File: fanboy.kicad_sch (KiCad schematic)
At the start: 51 parts, among them J1 XT30, J2 USB_C_Receptacle_USB2.0, J3 Conn_01x04, J4 Conn_01x04, SW1 GT-TC029B-H025-L1N, SW2 GT-TC029B-H025-L1N, U1 TPD1E05U06DYA, U2 TPD1E05U06DYA, U3 W25Q16JVUXIQ TR, U4 TLV1117LV33DCYR, U5 EMC2302, U6 RP2040, U7 SK6812, Y1 12MHz

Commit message: finished routing, added render and readme
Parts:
- removed C1, C2: 30pF, Capacitor_SMD:C_0402_1005Metric, symbol Device:C
- removed C10, C3, C5, C9: 1uF, Capacitor_SMD:C_0402_1005Metric, symbol Device:C
- removed C11, C12, C13, C15, C16, C17, C18, C4, C7, C8: 0.1uF, Capacitor_SMD:C_0402_1005Metric, symbol Device:C
- removed D1: SMAJ6.0A, Diode_SMD:D_SMB, symbol Diode:SMAJ6.0A
- removed J2: USB_C_Receptacle_USB2.0, aditBoard:USB_C_Receptacle_GCT_USB4105-xx-A_16P_TopMnt_Horizontal, symbol aditBoard:USB_C_Receptacle_USB2.0
- removed R1: 10k, Resistor_SMD:R_0402_1005Metric, symbol Device:R_US
- removed R11, R12: 4.7k, Resistor_SMD:R_0402_1005Metric, symbol Device:R_US
- removed R2, R3: 5.1k, Resistor_SMD:R_0402_1005Metric, symbol Device:R_US
- removed R4: 1k, Resistor_SMD:R_0402_1005Metric, symbol Device:R_US
- removed R5: 49.9k, Resistor_SMD:R_0402_1005Metric, symbol Device:R_US
- removed R7, R8: 33, Resistor_SMD:R_0402_1005Metric, symbol Device:R_US
- removed TP4: TestPoint, TestPoint:TestPoint_Pad_D1.0mm, symbol Connector:TestPoint
- removed U1, U2: TPD1E05U06DYA, Diode_SMD:D_SOD-523, symbol Power_Protection:TPD1E05U06DYA
- removed U3: W25Q16JVUXIQ TR, emberone:USON-8_UX_2x3x0p6_WIN, symbol emberone:W25Q16JVUXIQ_TR
- removed U4: TLV1117LV33DCYR, emberone:VREG_TLV1117LV33DCYR, symbol emberone:TLV1117LV33DCYR
- removed U6: RP2040, Package_DFN_QFN:QFN-56-1EP_7x7mm_P0.4mm_EP3.2x3.2mm, symbol aditBoard:RP2040
- removed U7: SK6812, emberone:LED-SMD_4P-L4.0-W1.6-L, symbol athvfd:SK6812SIDE-A-RVS
- added C100, C101, C104, C105, C106, C107, C108, C109, C110, C99: 0.1uF, Capacitor_SMD:C_0402_1005Metric, symbol Device:C
- added C102, C103, C90, C98: 1uF, Capacitor_SMD:C_0402_1005Metric, symbol Device:C
- added C96, C97: 30pF, Capacitor_SMD:C_0402_1005Metric, symbol Device:C
- added J6: USB_C_Receptacle_USB2.0, aditBoard:USB_C_Receptacle_GCT_USB4105-xx-A_16P_TopMnt_Horizontal, symbol aditBoard:USB_C_Receptacle_USB2.0
- added R19, R20: 4.7k, Resistor_SMD:R_0402_1005Metric, symbol Device:R_US
- added R34: 49.9k, Resistor_SMD:R_0402_1005Metric, symbol Device:R_US
- added R50: 10k, Resistor_SMD:R_0402_1005Metric, symbol Device:R_US
- added R51, R52: 5.1k, Resistor_SMD:R_0402_1005Metric, symbol Device:R_US
- added R53, R54: 33, Resistor_SMD:R_0402_1005Metric, symbol Device:R_US
- added R55: 1k, Resistor_SMD:R_0402_1005Metric, symbol Device:R_US
- added TP1, TP2: TestPoint, TestPoint:TestPoint_Pad_D1.0mm, symbol Connector:TestPoint
- added U10: TLV1117LV33DCYR, emberone:VREG_TLV1117LV33DCYR, symbol emberone:TLV1117LV33DCYR
- added U27: RP2040, Package_DFN_QFN:QFN-56-1EP_7x7mm_P0.4mm_EP3.2x3.2mm, symbol aditBoard:RP2040
- added U8: W25Q16JVUXIQ TR, emberone:USON-8_UX_2x3x0p6_WIN, symbol emberone:W25Q16JVUXIQ_TR
- added U9: SK6812, emberone:LED-SMD_4P-L4.0-W1.6-L, symbol athvfd:SK6812SIDE-A-RVS
- renumbered SW2 to SW1, SW1 to SW2
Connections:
- net 1V1: now also C100.2, C101.2, C102.2, U27.23 (DVDD), U27.45 (VREG_VOUT), U27.50 (DVDD)
- net 3V3: now also C103.2, C104.2, C105.2, C106.2, C107.2, C108.2, C109.2, C110.2, C98.1, C99.2, R19.1, R20.2, R34.2, R50.1, U10.2 (VOUT), U10.4 (VOUT), U27.1 (IOVDD), U27.10 (IOVDD), U27.22 (IOVDD), U27.33 (IOVDD), U27.42 (IOVDD), U27.43 (ADC_AVDD), U27.44 (VREG_IN), U27.48 (USB_VDD), U27.49 (IOVDD), U8.8 (VCC)
- net 5V: now also C90.1, J6.A4B9 (VBUS), J6.B4A9 (VBUS), U10.3 (VIN), U9.2 (VDD)
- net GND: now also TP3.1, C100.1, C101.1, C102.1, C103.1, C104.1, C105.1, C106.1, C107.1, C108.1, C109.1, C110.1, C90.2, C96.1, C97.1, C98.2, C99.1, J6.A1B12 (GND), J6.B1A12 (GND), J6.S1 (SHIELD), R51.1, R52.1, U10.1 (GND), U27.19 (TESTEN), U27.57 (GND), U8.4 (GND), U8.9 (EPAD), U9.4 (GND)
- net QSPI_SCLK: now also U27.52 (QSPI_SCLK), U8.6 (CLK)
- net QSPI_SD0: now also U27.53 (QSPI_SD0), U8.5 (DI(IO0))
- net QSPI_SD1: now also U27.55 (QSPI_SD1), U8.2 (DO(IO1))
- net QSPI_SD2: now also U27.54 (QSPI_SD2), U8.3 (/WP(IO2))
- net QSPI_SD3: now also U27.51 (QSPI_SD3), U8.7 (/HOLDOR/RESET(IO3))
- net QSPI_SS: now also R50.2, R55.1, U27.56 (QSPI_SS), U8.1 (/CS)
- net SCL: now also R20.1, TP1.1, U27.18 (GPIO15)
- net SDA: now also R19.2, TP2.1, U27.17 (GPIO14); no longer TP3.1
- net SWCLK: now also J6.A8 (SBU1), U27.24 (SWCLK)
- net SWD: now also J6.B8 (SBU2), U27.25 (SWD)
- net USB_DN: now also J6.A7 (D-), J6.B7 (D-), R54.1
- net USB_DP: now also J6.A6 (D+), J6.B6 (D+), R53.1
- net XIN: now also C97.2, U27.20 (XIN)
- net XOUT: now also C96.2, U27.21 (XOUT)
- net at SW2.1: now also R34.1, U27.26 (RUN)
- net at SW1.1: now also R55.2
- new net: R54.2, U27.46 (USB_DM)
- new net: J6.B5 (CC2), R52.2
- new net: U27.3 (GPIO1), U9.1 (DIN)
- new net: J6.A5 (CC1), R51.2
- new net: R53.2, U27.47 (USB_DP)
- new net THERM: U27.4 (GPIO2)
- no-connect marks 25 -> 17
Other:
- moved on the sheet: C14, C19, C20, C21, C6, J1, J3, J4, R10, R13, R6, R9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

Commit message: added BOM
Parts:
- R50: DK 311-10.0KLRCT-ND -> 311-10KJRCT-ND; PARTNO RC0402FR-0710KL -> RC0402JR-0710KL
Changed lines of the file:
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@@
 			)
 		)
-		(property "DK" "311-10.0KLRCT-ND"
+		(property "DK" "311-10KJRCT-ND"
 			(at 86.36 191.77 0)
 			(effects
@@
 			)
 		)
-		(property "PARTNO" "RC0402FR-0710KL"
+		(property "PARTNO" "RC0402JR-0710KL"
 			(at 86.36 191.77 0)
 			(effects

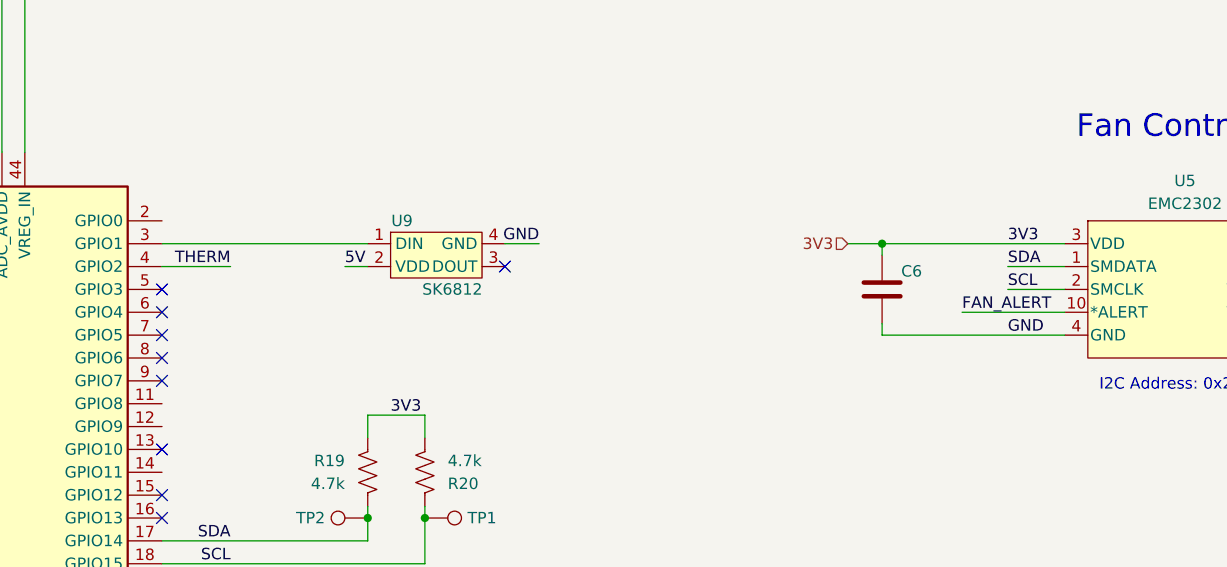
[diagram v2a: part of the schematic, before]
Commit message: connect FAN_ALERT to EMC2103 and add pullup
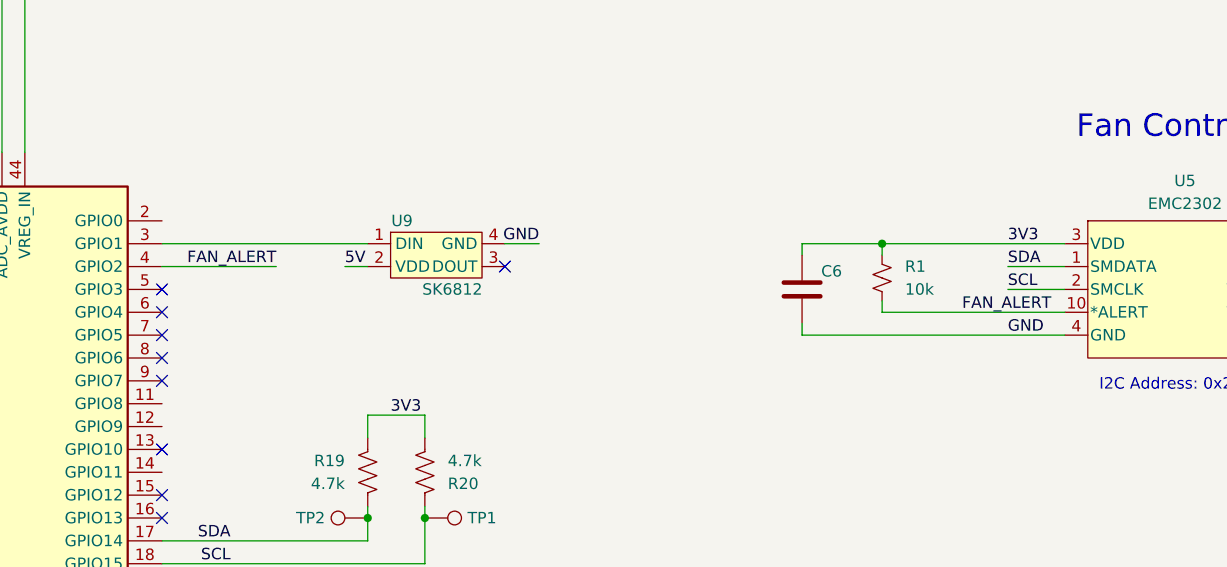
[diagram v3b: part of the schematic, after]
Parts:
- added R1: 10k, Resistor_SMD:R_0402_1005Metric, symbol Device:R_Small_US
- TP1: value TestPoint -> SCL
- TP2: value TestPoint -> SDA
- TP3: value TestPoint -> GND
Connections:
- net THERM is gone; now on net FAN_ALERT: U27.4 (GPIO2)
- net 3V3: now also R1.2
- net FAN_ALERT: now also R1.1
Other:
- moved on the sheet: C6
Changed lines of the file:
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@@
 	)
 	(junction
+		(at 312.42 107.95)
+		(diameter 0)
+		(color 0 0 0 0)
+	)
+	(junction
 		(at 142.24 166.37)
 		(diameter 0)
@@
 	)
 	(junction
-		(at 312.42 107.95)
-		(diameter 0)
-		(color 0 0 0 0)
-	)
-	(junction
 		(at 281.94 78.74)
 		(diameter 0)
@@
 	(wire
 		(pts
-			(xy 321.31 115.57) (xy 332.74 115.57)
+			(xy 163.83 115.57) (xy 168.91 115.57)
 		)
 		(stroke
@@
 	(wire
 		(pts
-			(xy 163.83 115.57) (xy 168.91 115.57)
+			(xy 339.09 161.29) (xy 345.44 161.29)
 		)
 		(stroke
@@
 	(wire
 		(pts
-			(xy 339.09 161.29) (xy 345.44 161.29)
+			(xy 259.08 68.58) (xy 259.08 69.85)
 		)
 		(stroke
@@
 	(wire
 		(pts
-			(xy 259.08 68.58) (xy 259.08 69.85)
+			(xy 312.42 107.95) (xy 312.42 109.22)
 		)
 		(stroke
@@
 	(wire
 		(pts
-			(xy 308.61 107.95) (xy 312.42 107.95)
-		)
-		(stroke
-			(width 0)
-			(type default)
-		)
-	)
-	(wire
-		(pts
 			(xy 88.9 124.46) (xy 76.2 124.46)
 		)
@@
 	(wire
 		(pts
-			(xy 312.42 118.11) (xy 332.74 118.11)
+			(xy 303.53 118.11) (xy 332.74 118.11)
 		)
 		(stroke
@@
 	(wire
 		(pts
-			(xy 312.42 107.95) (xy 312.42 109.22)
+			(xy 303.53 107.95) (xy 303.53 109.22)
 		)
 		(stroke
@@
 	(wire
 		(pts
+			(xy 312.42 114.3) (xy 312.42 115.57)
+		)
+		(stroke
+			(width 0)
+			(type default)
+		)
+	)
+	(wire
+		(pts
 			(xy 163.83 113.03) (xy 168.91 113.03)
 		)
@@
 	(wire
 		(pts
+			(xy 312.42 107.95) (xy 332.74 107.95)
+		)
+		(stroke
+			(width 0)
+			(type default)
+		)
+	)
+	(wire
+		(pts
 			(xy 351.79 157.48) (xy 351.79 158.75)
 		)
@@
 	(wire
 		(pts
-			(xy 312.42 107.95) (xy 332.74 107.95)
+			(xy 303.53 107.95) (xy 312.42 107.95)
 		)
 		(stroke
@@
 	(wire
 		(pts
-			(xy 312.42 116.84) (xy 312.42 118.11)
+			(xy 303.53 116.84) (xy 303.53 118.11)
 		)
 		(stroke
@@
 	(wire
 		(pts
-			(xy 232.41 110.49) (xy 240.03 110.49)
+			(xy 232.41 110.49) (xy 245.11 110.49)
 		)
 		(stroke
@@
 	(wire
 		(pts
+			(xy 312.42 115.57) (xy 332.74 115.57)
+		)
+		(stroke
+			(width 0)
+			(type default)
+		)
+	)
+	(wire
+		(pts
 			(xy 147.32 200.66) (xy 147.32 205.74)
 		)
@@
 		)
 	)
+	(label "FAN_ALERT"
+		(at 245.11 110.49 180)
+		(effects
+			(font
+				(size 1.27 1.27)
+			)
+			(justify right bottom)
+		)
+	)
 	(label "5V"
 		(at 350.52 186.69 0)
@@
 		)
 	)
-	(label "THERM"
-		(at 240.03 110.49 180)
-		(effects
-			(font
-				(size 1.27 1.27)
-			)
-			(justify right bottom)
-		)
-	)
 	(label "3V3"
 		(at 172.72 92.71 0)
@@
 		)
 	)
-	(hierarchical_label "3V3"
-		(shape input)
-		(at 308.61 107.95 180)
-		(effects
-			(font
-				(size 1.27 1.27)
-			)
-			(justify right)
-		)
-	)
 	(symbol
 		(lib_id "bitaxe:EMC2302-2-AIZL-TR")
@@
 			)
 		)
-		(property "Value" "TestPoint"
+		(property "Value" "GND"
 			(at 267.335 146.0501 90)
 			(effects
@@
 	(symbol
 		(lib_id "Device:C")
-		(at 312.42 113.03 0)
+		(at 303.53 113.03 0)
 		(mirror y)
 		(unit 1)
@@
 		(dnp no)
 		(property "Reference" "C6"
-			(at 316.865 111.76 0)
+			(at 307.975 111.76 0)
 			(effects
 				(font
@@
 		)
 		(property "Value" "311-3342-1-ND"
-			(at 312.42 113.03 0)
+			(at 303.53 113.03 0)
 			(effects
 				(font
@@
 		)
 		(property "Footprint" "Capacitor_SMD:C_0402_1005Metric"
-			(at 312.42 113.03 0)
+			(at 303.53 113.03 0)
 			(effects
 				(font
@@
 		)
 		(property "Datasheet" ""
-			(at 312.42 113.03 0)
+			(at 303.53 113.03 0)
 			(effects
 				(font
@@
 		)
 		(property "Description" ""
-			(at 312.42 113.03 0)
+			(at 303.53 113.03 0)
 			(effects
 				(font
@@
 		)
 		(property "DK" "478-KGM05AR71C104KHCT-ND"
-			(at 312.42 113.03 0)
+			(at 303.53 113.03 0)
 			(effects
 				(font
@@
 		)
 		(property "PARTNO" "KGM05AR71C104KH"
-			(at 312.42 113.03 0)
+			(at 303.53 113.03 0)
 			(effects
 				(font
@@
 	)
 	(symbol
+		(lib_id "Device:R_Small_US")
+		(at 312.42 111.76 180)
+		(unit 1)
+		(exclude_from_sim no)
+		(in_bom yes)
+		(on_board yes)
+		(dnp no)
+		(fields_autoplaced yes)
+		(property "Reference" "R1"
+			(at 314.96 110.4899 0)
+			(effects
+				(font
+					(size 1.27 1.27)
+				)
+				(justify right)
+			)
+		)
+		(property "Value" "10k"
+			(at 314.96 113.0299 0)
+			(effects
+				(font
+					(size 1.27 1.27)
+				)
+				(justify right)
+			)
+		)
+		(property "Footprint" "Resistor_SMD:R_0402_1005Metric"
+			(at 312.42 111.76 0)
+			(effects
+				(font
+					(size 1.27 1.27)
+				)
+				(hide yes)
+			)
+		)
+		(property "Datasheet" "~"
+			(at 312.42 111.76 0)
+			(effects
+				(font
+					(size 1.27 1.27)
+				)
+				(hide yes)
+			)
+		)
+		(property "Description" "Resistor, small US symbol"
+			(at 312.42 111.76 0)
+			(effects
+				(font
+					(size 1.27 1.27)
+				)
+				(hide yes)
+			)
+		)
+		(property "DK" "311-10KJRCT-ND"
+			(at 312.42 111.76 0)
+			(effects
+				(font
+					(size 1.27 1.27)
+				)
+				(hide yes)
+			)
+		)
+		(property "PARTNO" "RC0402JR-0710KL"
+			(at 312.42 111.76 0)
+			(effects
+				(font
+					(size 1.27 1.27)
+				)
+				(hide yes)
+			)
+		)
+		(pin "1"
+		)
+		(pin "2"
+		)
+		(instances
+			(project "fanboy"
+				(path "/529b265c-87f6-4af8-8bf9-e0d6b0673888"
+					(reference "R1")
+					(unit 1)
+				)
+			)
+		)
+	)
+	(symbol
 		(lib_id "Device:C")
 		(at 171.45 73.66 180)
@@
 			)
 		)
-		(property "Value" "TestPoint"
+		(property "Value" "SDA"
 			(at 249.555 139.6999 90)
 			(effects
@@
 			)
 		)
-		(property "Value" "TestPoint"
+		(property "Value" "SCL"
 			(at 267.335 137.1601 90)
 			(effects

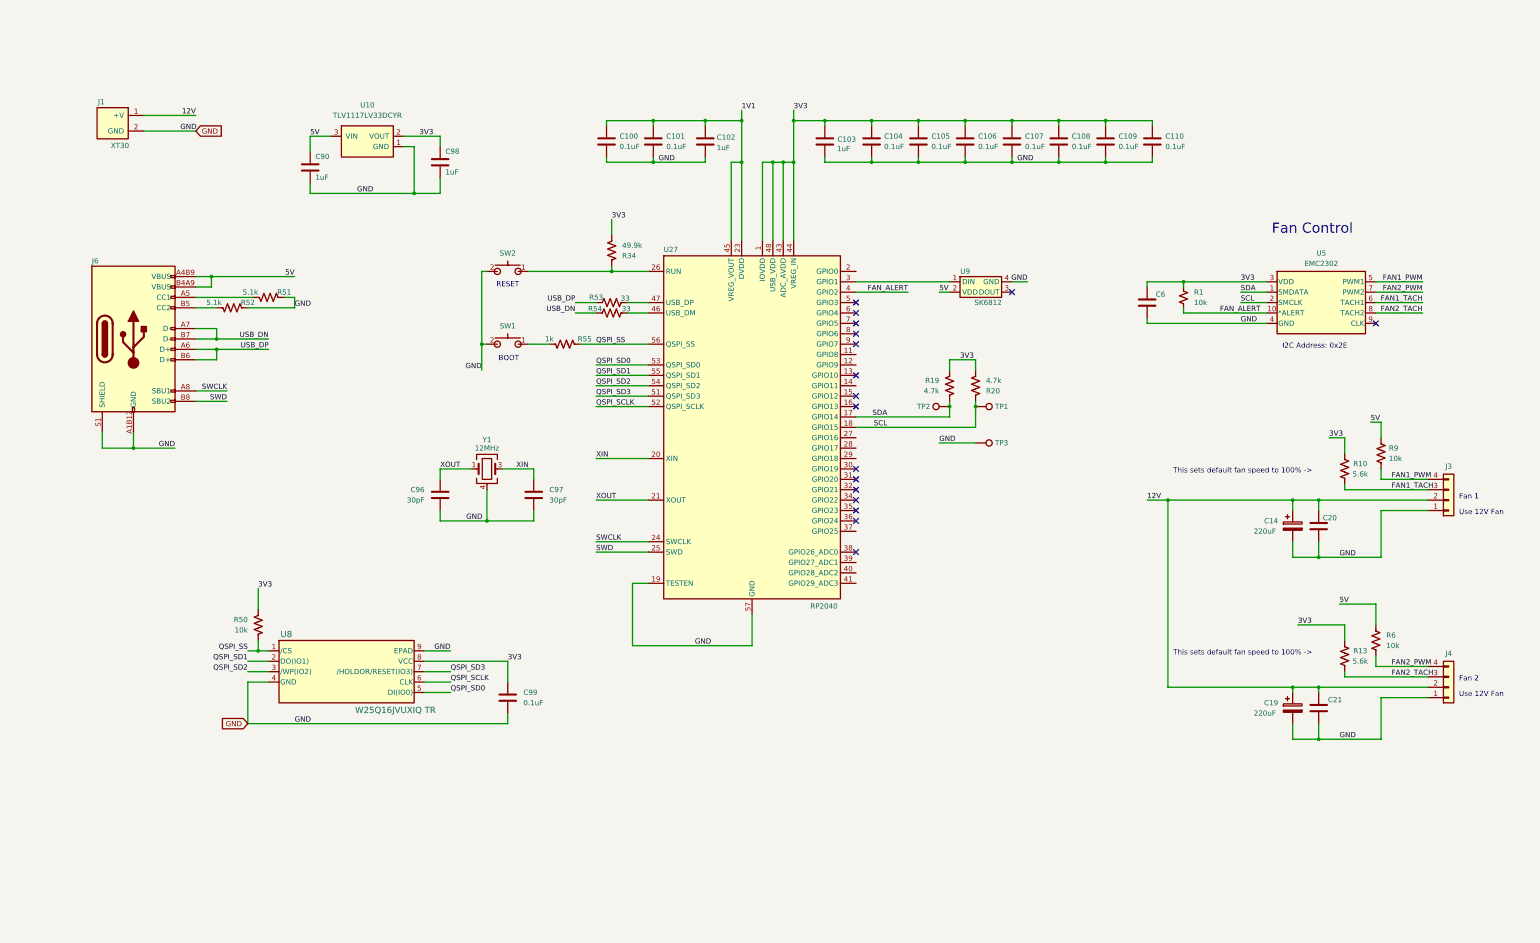
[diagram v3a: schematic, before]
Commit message: moved schematic symbols into separate library. added checked gerbers
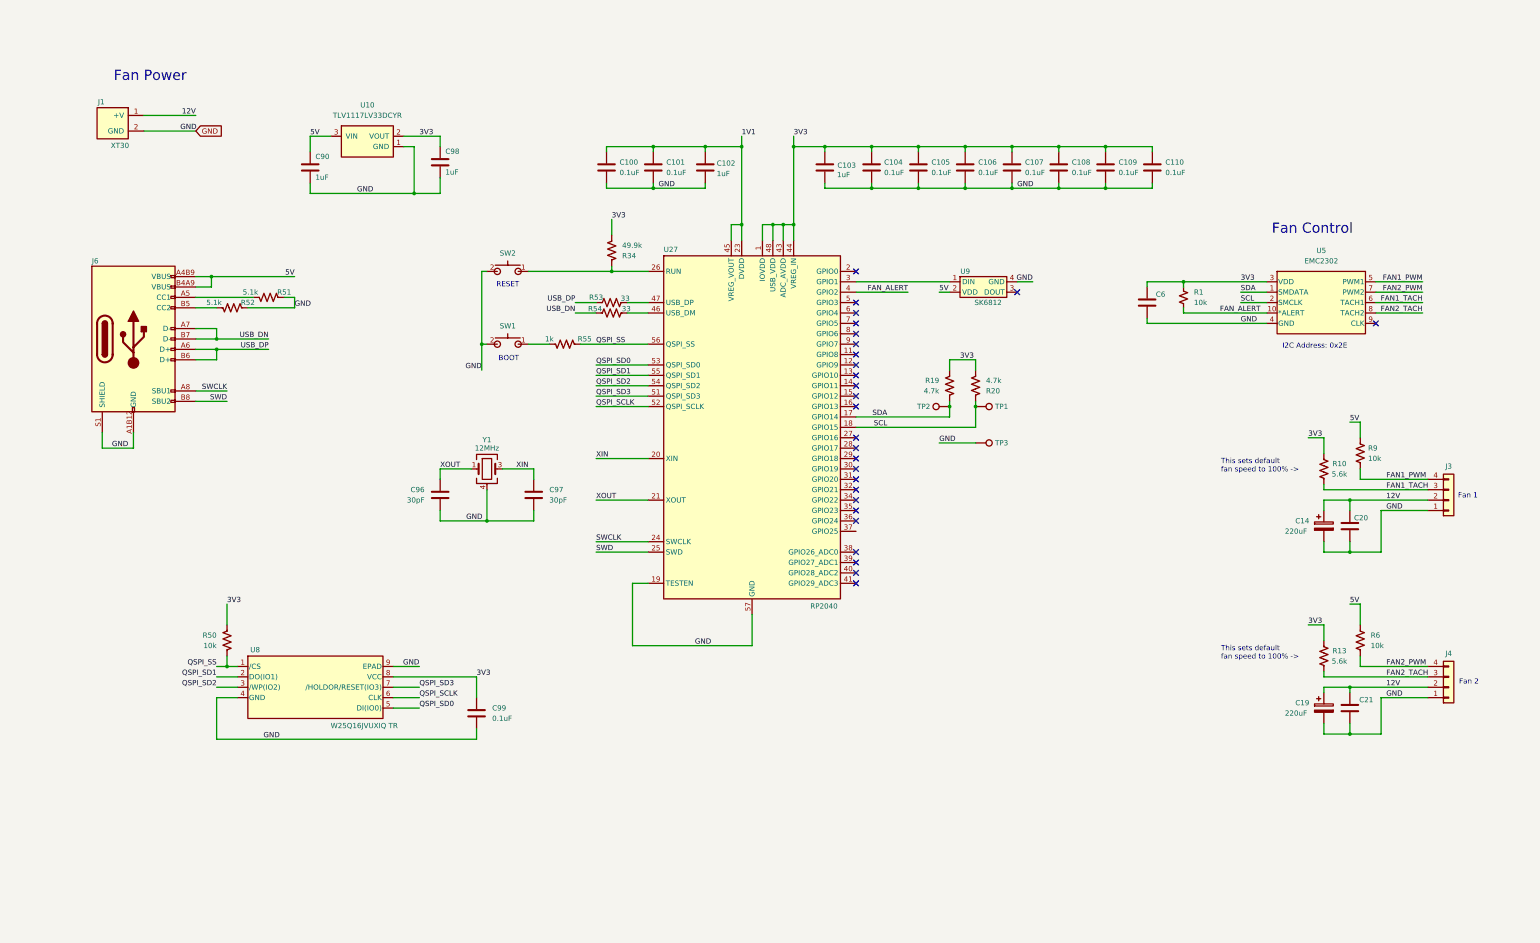
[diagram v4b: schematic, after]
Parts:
- J6: symbol aditBoard:USB_C_Receptacle_USB2.0 -> fanboy:USB_C_Receptacle_USB2.0
- U10: symbol emberone:TLV1117LV33DCYR -> fanboy:TLV1117LV33DCYR
- U5: symbol bitaxe:EMC2302-2-AIZL-TR -> fanboy:EMC2302-2-AIZL-TR
- U8: symbol emberone:W25Q16JVUXIQ_TR -> fanboy:W25Q16JVUXIQ_TR
- U9: symbol athvfd:SK6812SIDE-A-RVS -> fanboy:SK6812SIDE-A-RVS
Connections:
- no-connect marks 17 -> 27
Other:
- note added: "Fan Power"
- note removed: "Use 12V Fan"
- moved on the sheet: C100, C101, C102, C103, C104, C105, C106, C107, C108, C109, C110, C14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

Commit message: added mounting holes and fiducials. made board even 50x50mm. generated and checked gerbers
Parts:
- added FID1, FID2, FID3, FID4: Fiducial, bitaxe:Fiducial_1mm_Mask2mm, symbol Mechanical:Fiducial
- added H1, H2, H3, H4: MountingHole, MountingHole:MountingHole_3.5mm, symbol Mechanical:MountingHole
